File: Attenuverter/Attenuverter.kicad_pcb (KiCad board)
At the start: 2 copper layers, 30 x 100 mm, 49 parts, among them J1 AudioJack2_SwitchT, J2 AudioJack2_SwitchT, J3 AudioJack2_SwitchT, J4 AudioJack2_SwitchT, J5 AudioJack2_SwitchT, J6 AudioJack2_SwitchT, J7 Conn_02x05_Odd_Even, J8 AudioJack2_SwitchT, J9 AudioJack2_SwitchT, U1 TL084, U2 LM4040DBZ-5

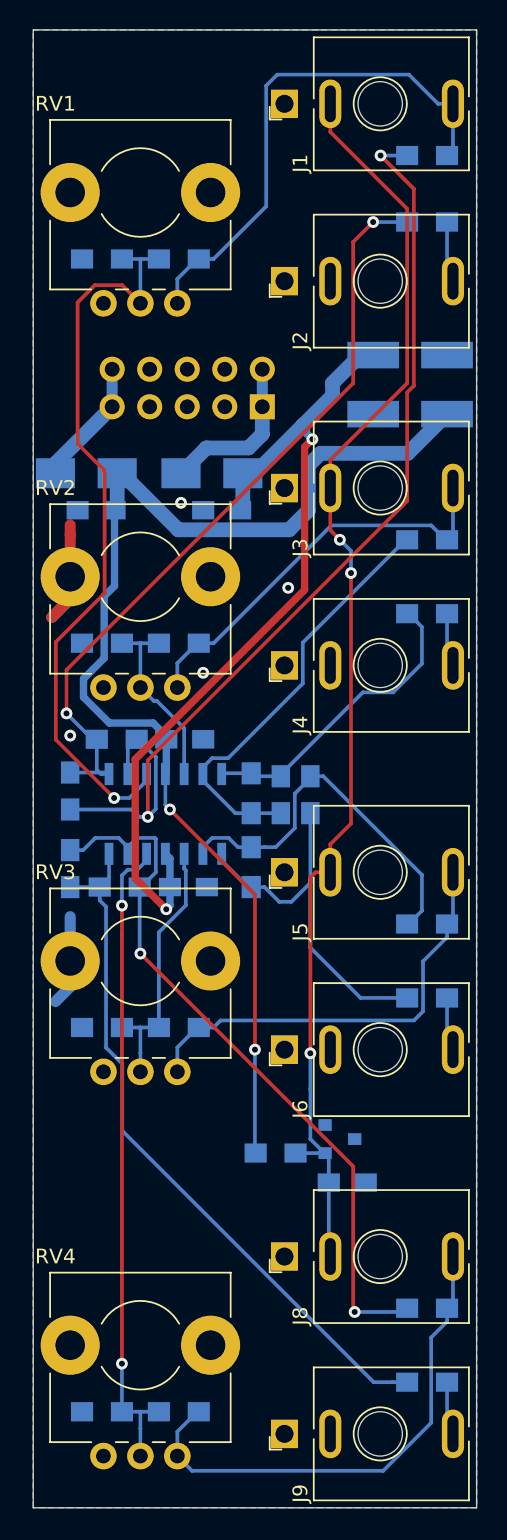
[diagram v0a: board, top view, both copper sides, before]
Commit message: Add input protection and migrate to KiCad 10
- Add input protection to the schematic and route it on the PCB
- Move the project to KiCad 10 format (Attenuverter.kicad_sch/.kicad_pcb)
- Nudge R6, R13, R14, and D11 (sub-mm) for alignment and even spacing
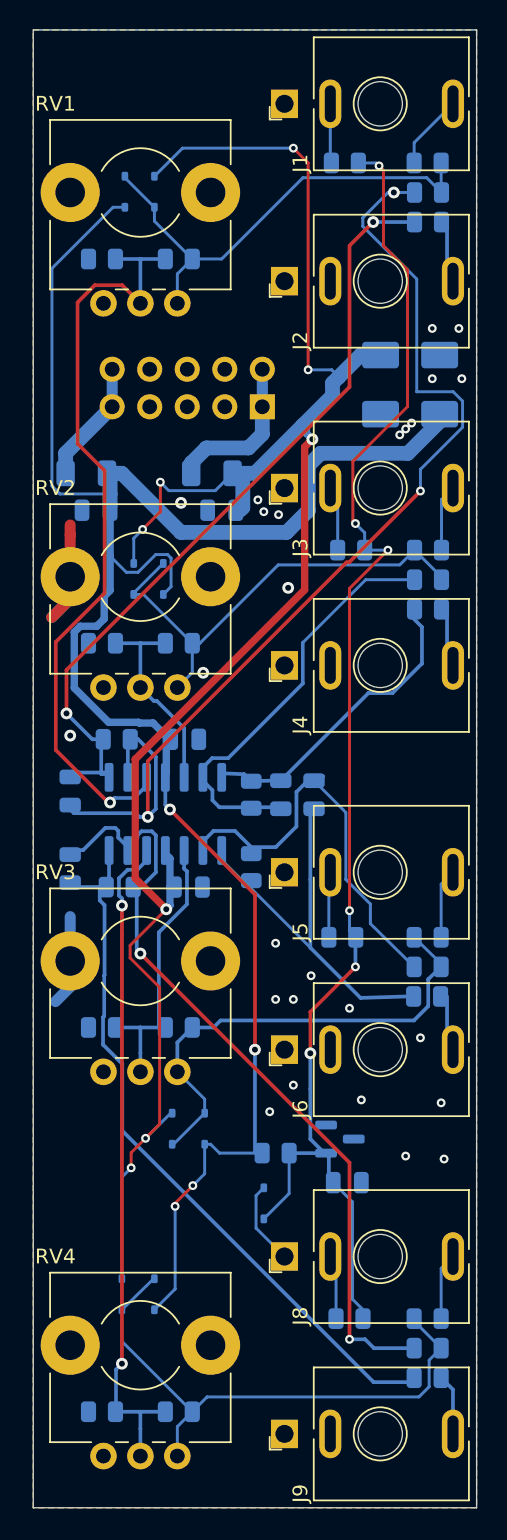
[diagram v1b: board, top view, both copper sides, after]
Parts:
- added D10: D, Diode_SMD:D_SOD-323, B.Cu at (108.2, 135.6)
- added D11: D, Diode_SMD:D_SOD-323, B.Cu at (106.0, 135.6)
- added D3: D, Diode_SMD:D_SOD-323, B.Cu at (115.6, 129.4)
- added D4: D, Diode_SMD:D_SOD-323, B.Cu at (108.2, 61.0)
- added D5: D, Diode_SMD:D_SOD-323, B.Cu at (106.2, 61.0)
- added D6: D, Diode_SMD:D_SOD-323, B.Cu at (108.8, 87.2)
- added D7: D, Diode_SMD:D_SOD-323, B.Cu at (106.8, 87.2)
- added D8: D, Diode_SMD:D_SOD-323, B.Cu at (111.6, 124.3)
- added D9: D, Diode_SMD:D_SOD-323, B.Cu at (109.4, 124.3)
- added R22: 1k, Resistor_SMD:R_0805_2012Metric, B.Cu at (121.1, 59.0)
- added R23: 1k, Resistor_SMD:R_0805_2012Metric, B.Cu at (121.5, 85.2)
- added R24: 1k, Resistor_SMD:R_0805_2012Metric, B.Cu at (120.9, 111.4)
- added R25: 1k, Resistor_SMD:R_0805_2012Metric, B.Cu at (121.4, 137.2)
- added R26: 1k, Resistor_SMD:R_0805_2012Metric, B.Cu at (126.7, 59.0)
- added R27: 1k, Resistor_SMD:R_0805_2012Metric, B.Cu at (126.7, 85.2)
- added R28: 1k, Resistor_SMD:R_0805_2012Metric, B.Cu at (126.7, 111.4)
- added R29: 1k, Resistor_SMD:R_0805_2012Metric, B.Cu at (126.7, 137.2)
- C1, C2, C3, C4, C5, C6, C7, C8, C9: footprint Capacitors_SMD:C_0805_HandSoldering -> Capacitor_SMD:C_0805_2012Metric
- D1, D2: footprint Diodes_SMD:D_SMA_Handsoldering -> Diode_SMD:D_SMA
- F1, F2: footprint Fuse_Holders_and_Fuses:Fuse_SMD1206_HandSoldering -> Fuse:Fuse_1206_3216Metric
- R1, R10, R11, R12, R13, R15, R16, R17, R18, R2, R20, R21, R4, R5, R6, R7, R9: footprint Resistors_SMD:R_0805_HandSoldering -> Resistor_SMD:R_0805_2012Metric
- R14, R19, R3, R8: value 100 -> 1k; footprint Resistors_SMD:R_0805_HandSoldering -> Resistor_SMD:R_0805_2012Metric
- U1: footprint Housings_SOIC:SOIC-14_3.9x8.7mm_Pitch1.27mm -> Package_SO:SOIC-14_3.9x8.7mm_P1.27mm
- U2: footprint TO_SOT_Packages_SMD:SOT-23 -> Package_TO_SOT_SMD:SOT-23
- moved R13 2.90 mm to (126.7, 113.4)
- moved R7 2.70 mm to (126.7, 87.2)
- moved R18 2.70 mm to (126.7, 139.2)
- moved R2 2.50 mm to (126.7, 61.0)
- moved R8 0.31 mm to (126.7, 89.2)
- moved R19 0.30 mm to (126.7, 141.2)
- moved C3 0.25 mm to (119.0, 101.8)
- moved R14 0.10 mm to (126.7, 115.4)
- moved R6 0.10 mm to (114.8, 101.8)
- moved R3 0.06 mm to (126.7, 63.0)
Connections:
- J1 pad T: Net-(J1-PadT) -> Net-(J1-~-PadT)
- J1 pad TN: +5V -> Net-(J1-~-PadTN)
- J2 pad TN: Net-(J2-PadTN) -> unconnected-(J2-~-PadTN)
- J3 pad T: Net-(J3-PadT) -> Net-(J3-~-PadT)
- J3 pad TN: +5V -> Net-(J3-~-PadTN)
- J4 pad TN: Net-(J4-PadTN) -> unconnected-(J4-~-PadTN)
- J5 pad T: Net-(J5-PadT) -> Net-(J5-~-PadT)
- J5 pad TN: +5V -> Net-(J5-~-PadTN)
- J6 pad TN: Net-(J6-PadTN) -> unconnected-(J6-~-PadTN)
- J8 pad T: Net-(J8-PadT) -> Net-(J8-~-PadT)
- J8 pad TN: +5V -> Net-(J8-~-PadTN)
- J9 pad TN: Net-(J9-PadTN) -> unconnected-(J9-~-PadTN)
- R13 pad 2: Net-(J5-PadT) -> Net-(D8-A)
- R15 pad 2: Net-(J5-PadT) -> Net-(D8-A)
- R18 pad 2: Net-(J8-PadT) -> Net-(D10-A)
- R2 pad 2: Net-(J1-PadT) -> Net-(D4-K)
- R20 pad 2: Net-(J8-PadT) -> Net-(D10-A)
- R4 pad 2: Net-(J1-PadT) -> Net-(D4-K)
- R7 pad 2: Net-(J3-PadT) -> Net-(D6-A)
- R9 pad 2: Net-(J3-PadT) -> Net-(D6-A)
- RV1 pad 1: Net-(J1-PadT) -> Net-(D4-K)
- RV2 pad 1: Net-(J3-PadT) -> Net-(D6-A)
- RV3 pad 1: Net-(J5-PadT) -> Net-(D8-A)
- RV4 pad 1: Net-(J8-PadT) -> Net-(D10-A)
- U2 pad 3: (no net) -> unconnected-(U2-NC-Pad3)
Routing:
- net -12V: track 58.0 -> 128.2 mm, vias 2 -> 8
- net +12V: track 82.5 -> 133.6 mm, vias 2 -> 4
- net Net-(D10-A): track 0.00 -> 37.8 mm
- net Net-(J1-PadT): track 35.3 -> 0.00 mm
- net Net-(J8-PadT): track 34.5 -> 0.00 mm
- net Net-(D4-K): track 0.00 -> 32.5 mm
- net Net-(D8-A): track 0.00 -> 32.4 mm
- net Net-(D6-A): track 0.00 -> 32.2 mm
- net Net-(J5-PadT): track 29.5 -> 0.00 mm
- net Net-(J3-PadT): track 27.8 -> 0.00 mm
- net +5V: track 87.2 -> 94.2 mm, vias 3 -> 6
- net GND: track 17.4 -> 23.1 mm, vias 4 -> 26
- net Net-(J1-~-PadT): track 0.00 -> 5.09 mm
- net Net-(J5-~-PadT): track 0.00 -> 4.73 mm
- net Net-(J8-~-PadT): track 0.00 -> 4.53 mm
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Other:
- net class Default removed
- net class Power removed
